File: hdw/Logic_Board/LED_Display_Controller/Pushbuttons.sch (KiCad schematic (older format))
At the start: 20 parts, among them J1401 Encoder Ext, SW1401 Display Enable, SW1402 Brightness/Enable, U1401 MAX6816, U1402 74LVC2G14, U1403 74LVC1G79

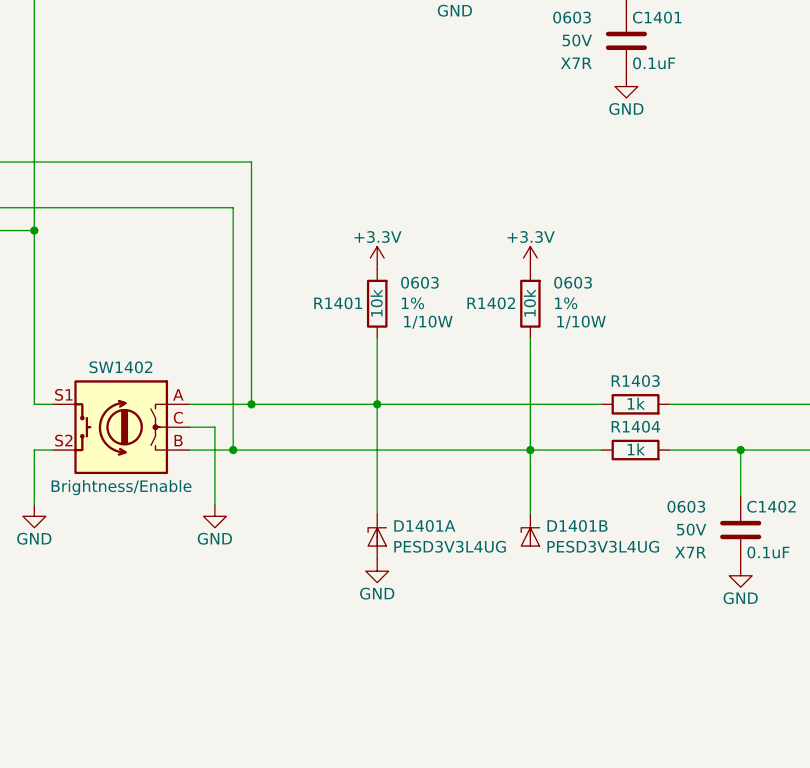
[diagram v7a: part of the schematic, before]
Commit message: First pass of placing parts
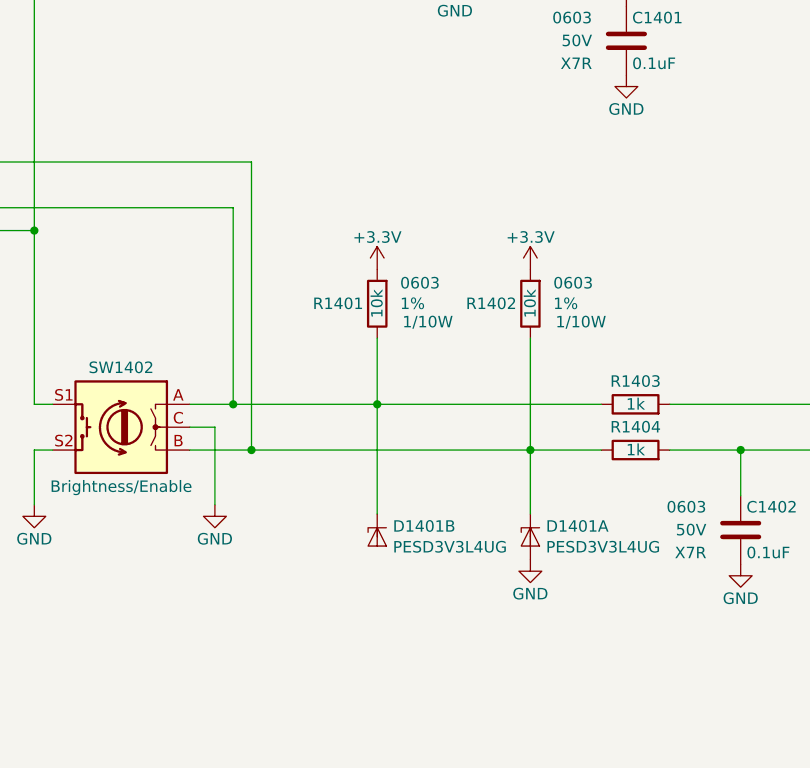
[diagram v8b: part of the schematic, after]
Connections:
- net at R1401.2, R1403.2, SW1402.A: now also D1401.3 (K2), J1401.3 (Pin_3); no longer D1401.1 (K1), J1401.1 (Pin_1)
- net at R1402.2, R1404.2, SW1402.B: now also D1401.1 (K1), J1401.1 (Pin_1); no longer D1401.3 (K2), J1401.3 (Pin_3)
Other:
- moved on the sheet: D1401A, D1401B
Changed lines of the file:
@@
 	4070 4390 3090 4390
-Wire Wire Line
-	2270 4590 2460 4590
 Wire Wire Line
 	3090 4100 3090 4390
@@
 L LED_Display_Local_Library:PESD3V3L4UG D1401
 U 1 1 5BF48679
+P 3760 4970
+F 0 "D1401" V 3714 5038 50  0000 L CNN
+F 1 "PESD3V3L4UG" V 3805 5038 50  0000 L CNN
+F 2 "TO_SOT_Packages_SMD:SOT-353_SC-70-5" H 3760 4970 50  0001 C CNN
+F 3 "http://www.nxp.com/documents/data_sheet/PESDXL4UF_G_W.pdf" H 3760 4970 50  0001 C CNN
+F 4 "1727-3827-1-ND" H 670 0   50  0001 C CNN "Digi-Key PN"
+	1    3760 4970
+	0    1    1    0
+$EndComp
+$Comp
+L power:GND #PWR01406
+U 1 1 5BF48715
+P 3760 5070
+F 0 "#PWR01406" H 3760 4820 50  0001 C CNN
+F 1 "GND" H 3760 4920 50  0000 C CNN
+F 2 "" H 3760 5070 50  0001 C CNN
+F 3 "" H 3760 5070 50  0001 C CNN
+	1    3760 5070
+	1    0    0    -1
+$EndComp
+$Comp
+L LED_Display_Local_Library:PESD3V3L4UG D1401
+U 2 1 5BF4A271
 P 3090 4970
 F 0 "D1401" V 3044 5038 50  0000 L CNN
@@
 F 2 "TO_SOT_Packages_SMD:SOT-353_SC-70-5" H 3090 4970 50  0001 C CNN
 F 3 "http://www.nxp.com/documents/data_sheet/PESDXL4UF_G_W.pdf" H 3090 4970 50  0001 C CNN
-F 4 "1727-3827-1-ND" H 0   0   50  0001 C CNN "Digi-Key PN"
-	1    3090 4970
-	0    1    1    0
-$EndComp
-$Comp
-L power:GND #PWR01406
-U 1 1 5BF48715
-P 3090 5070
-F 0 "#PWR01406" H 3090 4820 50  0001 C CNN
-F 1 "GND" H 3090 4920 50  0000 C CNN
-F 2 "" H 3090 5070 50  0001 C CNN
-F 3 "" H 3090 5070 50  0001 C CNN
-	1    3090 5070
-	1    0    0    -1
-$EndComp
-$Comp
-L LED_Display_Local_Library:PESD3V3L4UG D1401
-U 2 1 5BF4A271
-P 3760 4970
-F 0 "D1401" V 3714 5038 50  0000 L CNN
-F 1 "PESD3V3L4UG" V 3805 5038 50  0000 L CNN
-F 2 "TO_SOT_Packages_SMD:SOT-353_SC-70-5" H 3760 4970 50  0001 C CNN
-F 3 "http://www.nxp.com/documents/data_sheet/PESDXL4UF_G_W.pdf" H 3760 4970 50  0001 C CNN
-F 4 "1727-3827-1-ND" H 0   0   50  0001 C CNN "Digi-Key PN"
-	2    3760 4970
+F 4 "1727-3827-1-ND" H -670 0   50  0001 C CNN "Digi-Key PN"
+	2    3090 4970
 	0    1    1    0
 $EndComp
@@
 	1240 3530 2460 3530
 Wire Wire Line
-	2460 3530 2460 4590
-Wire Wire Line
 	1360 3730 1360 3430
 Wire Wire Line
@@
 Wire Wire Line
 	1240 3330 2540 3330
-Wire Wire Line
-	2540 3330 2540 4390
-Wire Wire Line
-	2540 4390 2270 4390
 Text Notes 550  700  0    100  ~ 20
 14. Pushbuttons
@@
 Connection ~ 2010 2170
 Wire Wire Line
-	3090 4390 2540 4390
-Connection ~ 2540 4390
-Wire Wire Line
-	3760 4590 2460 4590
-Connection ~ 2460 4590
+	2270 4590 2540 4590
+Wire Wire Line
+	2460 3530 2460 4390
+Connection ~ 2460 4390
+Wire Wire Line
+	2460 4390 2270 4390
+Wire Wire Line
+	2460 4390 3090 4390
+Wire Wire Line
+	2540 3330 2540 4590
+Connection ~ 2540 4590
+Wire Wire Line
+	2540 4590 3760 4590
 $EndSCHEMATC
